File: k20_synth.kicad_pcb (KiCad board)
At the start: 2 copper layers, 98 parts, among them J1 USB_OTG_PWR, J2 MIDI-DIN-5, J3 Conn_02x10_Odd_Even, J4 Screw_Terminal_01x02, SW1 SW_Push_Dual_x2, SW2 SW_Push_Dual_x2, SW3 SW_Push_Dual_x2, U1 H11L1, U10 MCP6024, U2 MCP1702T-3302E/CB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

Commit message: so many crashes
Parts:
- moved U7 124.6 mm to (31.6, 170.3)
- moved C27 117.1 mm to (33.7, 180.8)
- moved R37 113.9 mm to (42.3, 185.5)
- moved R31 107.1 mm to (63.5, 157.4), turned to 90 degrees
- moved R36 106.2 mm to (38.4, 182.4)
- moved R35 105.2 mm to (66.5, 157.4), turned to 90 degrees
- moved R34 101.7 mm to (65.0, 157.4), turned to 90 degrees
- moved R32 99.9 mm to (62.0, 157.4), turned to 270 degrees
- moved R30 94.3 mm to (60.5, 157.4), turned to 270 degrees
- moved C28 93.6 mm to (57.8, 153.7), turned to 180 degrees
- moved R33 90.6 mm to (68.1, 157.4), turned to 90 degrees
- moved U6 80.8 mm to (55.5, 157.4)
- moved U10 35.7 mm to (121.3, 163.6)
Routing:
- net Net-(U6-Pad11): track 0.00 -> 6.45 mm
- net Net-(U6-Pad1): track 0.00 -> 6.18 mm
- net GND: track 66.9 -> 72.5 mm, vias 7 -> 8

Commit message: Finished layout, hopefully it works
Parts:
- added C29: 0.1uF, k20_dev_board:C_0603, F.Cu at (183.3, 101.9)
- J4: value Screw_Terminal_01x02 -> Spk_Screw_Terminal_01x02
- moved U7 180.9 mm to (208.3, 131.8), turned to 270 degrees
- moved R36 174.1 mm to (204.0, 128.6), turned to 90 degrees
- moved C27 171.7 mm to (194.9, 121.9), turned to 180 degrees
- moved R37 170.0 mm to (202.4, 128.6), turned to 270 degrees
- moved C28 143.8 mm to (199.4, 128.6), turned to 90 degrees
- moved U6 143.7 mm to (195.8, 126.6), turned to 270 degrees
- moved R30 139.3 mm to (197.4, 131.8), turned to 180 degrees
- moved R32 137.5 mm to (197.4, 133.3), turned to 180 degrees
- moved R31 135.7 mm to (197.4, 134.8), turned to 0 degrees
- moved R34 134.0 mm to (197.4, 136.3), turned to 0 degrees
- moved R35 132.3 mm to (197.4, 137.9), turned to 0 degrees
- moved R33 130.5 mm to (197.4, 139.4), turned to 0 degrees
- moved SW1 118.8 mm to (163.4, 99.6), turned to 180 degrees
- moved C26 117.3 mm to (217.1, 127.6)
- moved C24 115.0 mm to (212.0, 137.2), turned to 180 degrees
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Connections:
- R21 pad 2: /PTB2 -> /FTM1_CH1
- R22 pad 2: /PTB3 -> /FTM1_CH0
- SW1 pad 1: +3V3 -> /FTM1_CH1
- SW1 pad 3: /PTB2 -> +3V3
- SW2 pad 1: +3V3 -> /FTM1_CH0
- SW2 pad 3: /PTB3 -> +3V3
- SW3 pad 2: GND -> /~RESET
- SW3 pad 4: /~RESET -> GND
- U10 pad 12: Net-(R17-Pad1) -> /VREF_OUT
- U10 pad 13: Net-(R18-Pad1) -> Net-(R18-Pad2)
- U10 pad 14: Net-(R23-Pad2) -> Net-(R18-Pad2)
- U10 pad 5: /VREF_OUT -> Net-(R17-Pad1)
- U10 pad 6: Net-(R18-Pad2) -> Net-(R18-Pad1)
- U10 pad 7: Net-(R18-Pad2) -> Net-(R23-Pad2)
- U3 pad 44: /LED_BLUE -> Net-(U3-Pad44)
- U3 pad 45: /LED_GREEN -> Net-(U3-Pad45)
- U3 pad 46: /LED_RED -> Net-(U3-Pad46)
- U3 pad 62: /FTM0_CH5 -> /LED_BLUE
- U3 pad 63: /FTM0_CH6 -> /LED_GREEN
- U3 pad 64: /FTM0_CH7 -> /LED_RED
- U9 pad 5: Net-(J4-Pad1) -> Net-(J4-Pad2)
- U9 pad 8: Net-(J4-Pad2) -> Net-(J4-Pad1)
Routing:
- net +3V3: track 29.8 -> 122.0 mm, vias 2 -> 19
- net +5V: track 4.16 -> 95.7 mm, vias 0 -> 3
- net Net-(R23-Pad2): track 0.00 -> 64.4 mm, vias 0 -> 4
- net GND: track 72.5 -> 135.1 mm, vias 8 -> 26
- net /NORM_WAVEGEN: track 0.00 -> 52.1 mm, vias 0 -> 4
- net /JTAG_TCLK: track 0.00 -> 47.6 mm
- net /~RESET: track 0.00 -> 46.0 mm, vias 0 -> 2
- net /ADC0_DM3: track 0.00 -> 44.7 mm
- net /JTAG_TDI: track 0.00 -> 43.9 mm
- net Net-(R19-Pad1): track 0.00 -> 38.2 mm, vias 0 -> 2
- net /~JTAG_TRST: track 4.41 -> 40.6 mm, vias 0 -> 2
- net /JTAG_TDO: track 0.00 -> 35.2 mm, vias 0 -> 2
- net /JTAG_TMS: track 4.36 -> 38.9 mm
- net /ADC0_DP3: track 0.00 -> 34.5 mm
- net /VREF_OUT: track 0.00 -> 32.8 mm, vias 0 -> 2
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- added copper zone on B.Cu, net GND
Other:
- board outline added: 78.4 x 62.4 mm
- board text added: "SPK+"
- board text added: "SPK-"

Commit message: Added our names for posterity
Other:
- board text added: "William Lu Franton Lin Eclectronics FL2017"
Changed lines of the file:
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@@
     (area 146.165499 80.696999 224.738001 143.267501)
     (thickness 1.6)
-    (drawings 10)
+    (drawings 11)
     (tracks 750)
     (zones 0)
@@
     )
   )
+  (gr_text "William Lu\nFranton Lin\nEclectronics FL2017" (at 157.734 139.0904) (layer F.SilkS)
+    (effects (font (size 1 1) (thickness 0.25)) (justify left))
+  )
   (gr_text SPK+ (at 222.504 122.7455) (layer F.SilkS)

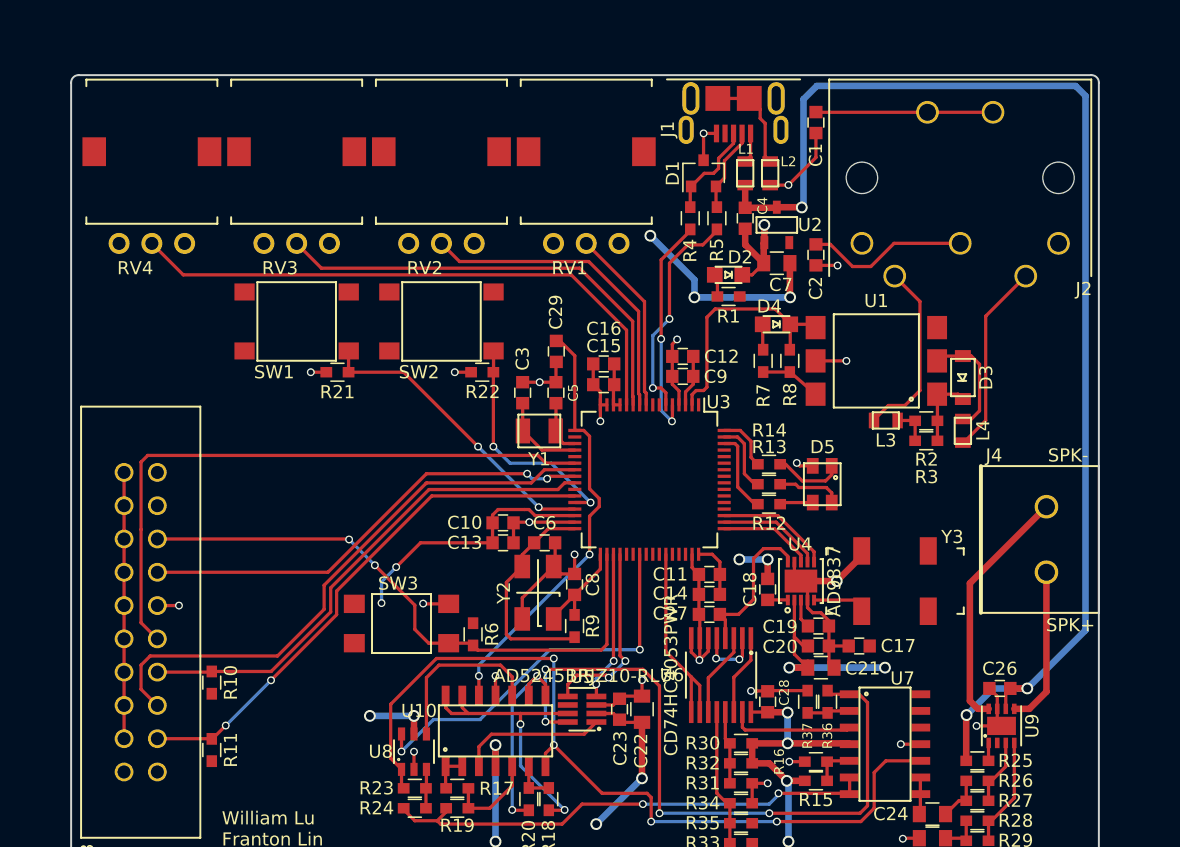
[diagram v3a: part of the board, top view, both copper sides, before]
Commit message: Fixed footprint masks, potentiometer footprints and spacing
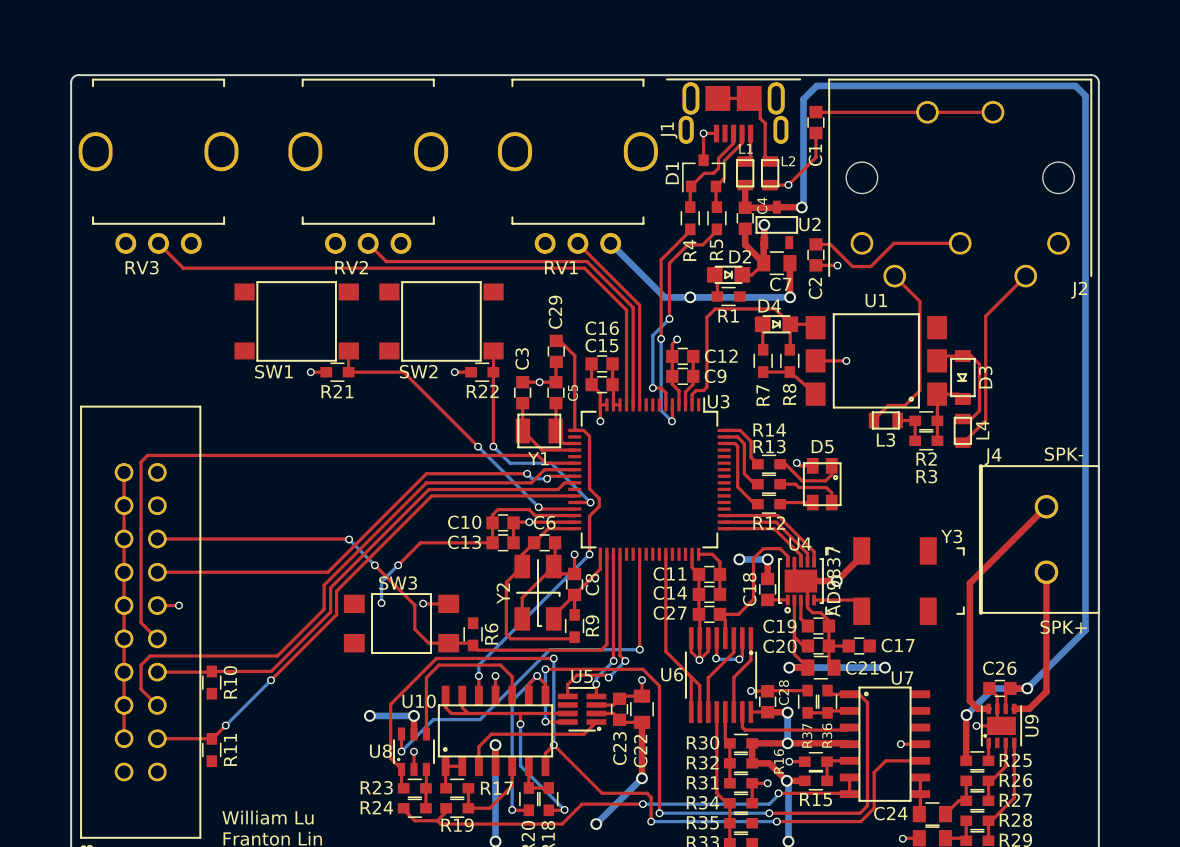
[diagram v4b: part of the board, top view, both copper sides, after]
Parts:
- removed RV4: POT, k20_dev_board:PTV09A-4020U
- moved RV3 10.5 mm to (152.9, 86.6)
- moved RV2 5.59 mm to (168.9, 86.6)
- moved RV1 0.63 mm to (184.9, 86.6)
- moved C15 0.13 mm to (186.8, 104.4)
- moved C16 0.13 mm to (186.8, 102.8)
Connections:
- RV1 pad 2: /ADC0_DP0 -> /ADC0_DM0
- RV2 pad 2: /ADC0_DM0 -> /ADC0_DP3
- RV3 pad 2: /ADC0_DP3 -> /ADC0_DM3
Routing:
- net /ADC0_DP0: track 14.2 -> 0.00 mm
- net /ADC0_DM0: track 24.4 -> 14.3 mm
- net /ADC0_DP3: track 34.5 -> 29.7 mm
- net +3V3: track 122.0 -> 124.1 mm, vias 19 -> 18
